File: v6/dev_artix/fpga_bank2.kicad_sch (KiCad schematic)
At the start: 37 parts, among them J401 AMD JTAG Header, U301 XC7A100T-CSG324

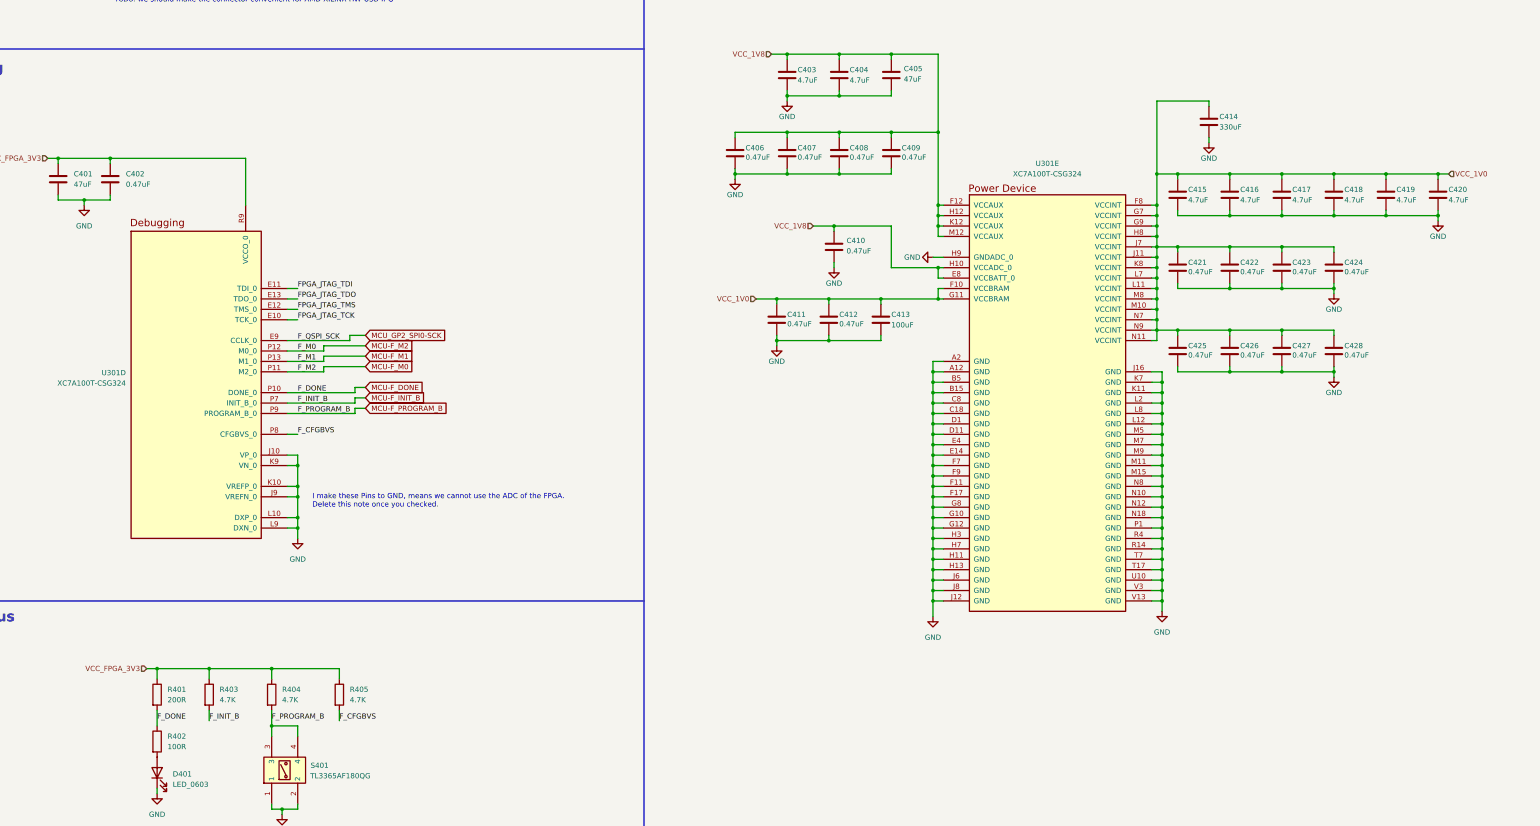
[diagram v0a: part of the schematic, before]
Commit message: Adapt numbers for easier ordering and assembling
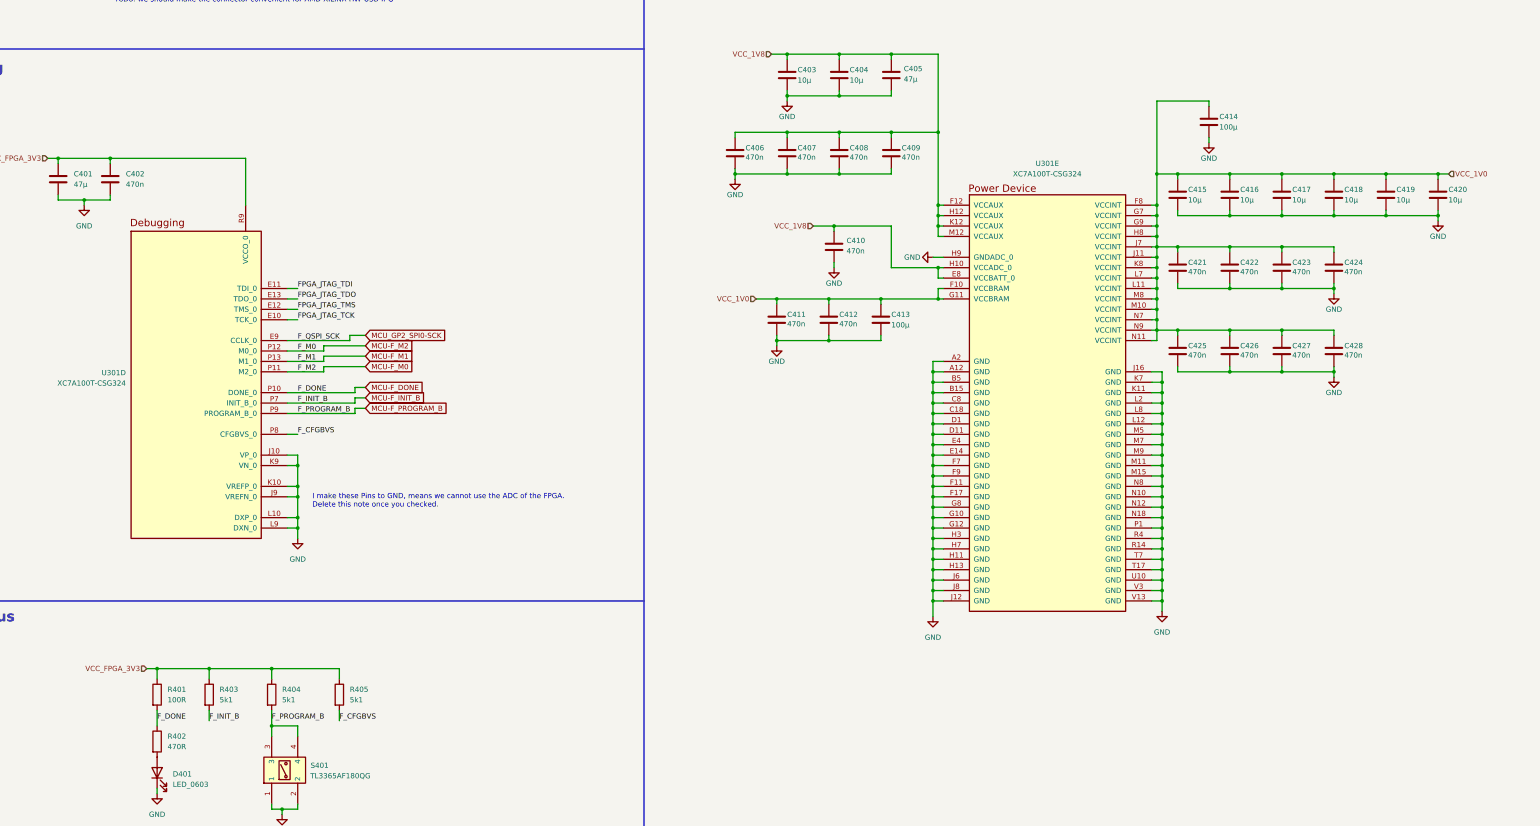
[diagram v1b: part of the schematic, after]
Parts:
- C401, C405: value 47uF -> 47µ
- C402, C406, C407, C408, C409, C410, C411, C412, C421, C422, C423, C424, C425, C426, C427, C428: value 0.47uF -> 470n
- C403, C404, C415, C416, C417, C418, C419, C420: value 4.7uF -> 10µ
- C413: value 100uF -> 100µ
- C414: value 330uF -> 100µ
- R401: value 200R -> 100R
- R402: value 100R -> 470R
- R403, R404, R405: value 4.7K -> 5k1
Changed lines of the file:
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@@
 			)
 		)
-		(property "Value" "100R"
+		(property "Value" "470R"
 			(at 74.93 252.7299 0)
 			(effects
@@
 			)
 		)
-		(property "Value" "47uF"
+		(property "Value" "47µ"
 			(at 254.508 89.916 0)
 			(effects
@@
 			)
 		)
-		(property "Value" "4.7uF"
+		(property "Value" "10µ"
 			(at 323.85 119.38 0)
 			(effects
@@
 			)
 		)
-		(property "Value" "0.47uF"
+		(property "Value" "470n"
 			(at 64.77 115.5699 0)
 			(effects
@@
 			)
 		)
-		(property "Value" "4.7uF"
+		(property "Value" "10µ"
 			(at 361.95 119.38 0)
 			(effects
@@
 			)
 		)
-		(property "Value" "4.7uF"
+		(property "Value" "10µ"
 			(at 336.55 119.38 0)
 			(effects
@@
 			)
 		)
-		(property "Value" "200R"
+		(property "Value" "100R"
 			(at 74.93 241.2999 0)
 			(effects
@@
 			)
 		)
-		(property "Value" "0.47uF"
+		(property "Value" "470n"
 			(at 241.3 108.966 0)
 			(effects
@@
 			)
 		)
-		(property "Value" "4.7K"
+		(property "Value" "5k1"
 			(at 87.63 241.2999 0)
 			(effects
@@
 			)
 		)
-		(property "Value" "4.7uF"
+		(property "Value" "10µ"
 			(at 241.3 90.17 0)
 			(effects
@@
 			)
 		)
-		(property "Value" "47uF"
+		(property "Value" "47µ"
 			(at 52.07 115.5699 0)
 			(effects
@@
 			)
 		)
-		(property "Value" "0.47uF"
+		(property "Value" "470n"
 			(at 361.95 157.226 0)
 			(effects
@@
 			)
 		)
-		(property "Value" "0.47uF"
+		(property "Value" "470n"
 			(at 349.25 157.226 0)
 			(effects
@@
 			)
 		)
-		(property "Value" "4.7K"
+		(property "Value" "5k1"
 			(at 102.87 241.2999 0)
 			(effects
@@
 			)
 		)
-		(property "Value" "0.47uF"
+		(property "Value" "470n"
 			(at 228.6 108.966 0)
 			(effects
@@
 			)
 		)
-		(property "Value" "0.47uF"
+		(property "Value" "470n"
 			(at 254 108.966 0)
 			(effects
@@
 			)
 		)
-		(property "Value" "4.7uF"
+		(property "Value" "10µ"
 			(at 228.6 90.17 0)
 			(effects
@@
 			)
 		)
-		(property "Value" "0.47uF"
+		(property "Value" "470n"
 			(at 238.76 149.606 0)
 			(effects
@@
 			)
 		)
-		(property "Value" "0.47uF"
+		(property "Value" "470n"
 			(at 240.538 131.826 0)
 			(effects
@@
 			)
 		)
-		(property "Value" "0.47uF"
+		(property "Value" "470n"
 			(at 215.9 108.966 0)
 			(effects
@@
 			)
 		)
-		(property "Value" "0.47uF"
+		(property "Value" "470n"
 			(at 349.25 136.906 0)
 			(effects
@@
 			)
 		)
-		(property "Value" "0.47uF"
+		(property "Value" "470n"
 			(at 336.55 136.906 0)
 			(effects
@@
 			)
 		)
-		(property "Value" "0.47uF"
+		(property "Value" "470n"
 			(at 361.95 136.906 0)
 			(effects
@@
 			)
 		)
-		(property "Value" "100uF"
+		(property "Value" "100µ"
 			(at 251.46 149.86 0)
 			(effects
@@
 			)
 		)
-		(property "Value" "0.47uF"
+		(property "Value" "470n"
 			(at 323.85 136.906 0)
 			(effects
@@
 			)
 		)
-		(property "Value" "4.7uF"
+		(property "Value" "10µ"
 			(at 387.35 119.38 0)
 			(effects
@@
 			)
 		)
-		(property "Value" "0.47uF"
+		(property "Value" "470n"
 			(at 323.85 157.226 0)
 			(effects
@@
 			)
 		)
-		(property "Value" "330uF"
+		(property "Value" "100µ"
 			(at 331.47 101.6 0)
 			(effects
@@
 			)
 		)
-		(property "Value" "0.47uF"
+		(property "Value" "470n"
 			(at 336.55 157.226 0)
 			(effects
@@
 			)
 		)
-		(property "Value" "4.7K"
+		(property "Value" "5k1"
 			(at 119.38 241.2999 0)
 			(effects
@@
 			)
 		)
-		(property "Value" "4.7uF"
+		(property "Value" "10µ"
 			(at 374.65 119.38 0)
 			(effects
@@
 			)
 		)
-		(property "Value" "0.47uF"
+		(property "Value" "470n"
 			(at 226.06 149.606 0)
 			(effects
@@
 			)
 		)
-		(property "Value" "4.7uF"
+		(property "Value" "10µ"
 			(at 349.25 119.38 0)
 			(effects
